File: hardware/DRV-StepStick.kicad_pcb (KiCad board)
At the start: 2 copper layers, 36.7 x 39.4 mm, 21 parts, among them J1 PCIe_Stepper, J2 Motor, J3 StepStickL, J4 StepStickR, J5 Conn_01x04, J6 SPI Mode, J7 Conn_01x02, U2 74LVC1G06

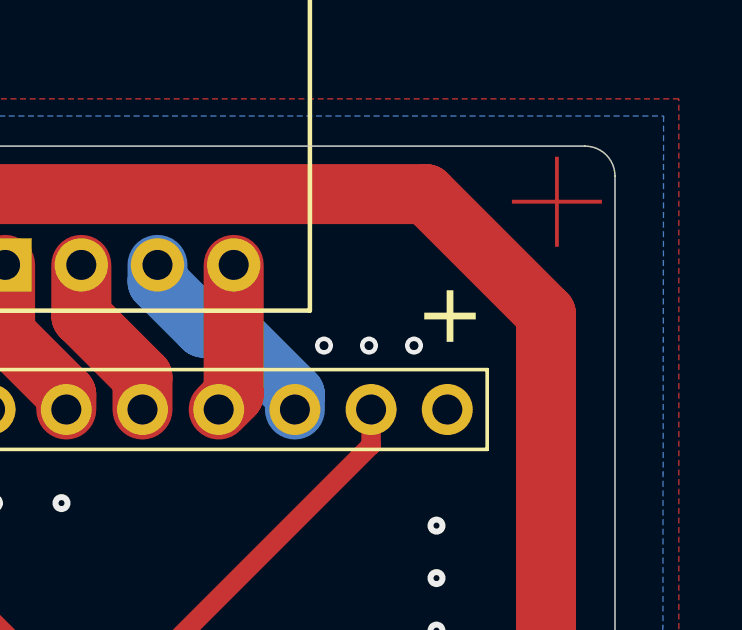
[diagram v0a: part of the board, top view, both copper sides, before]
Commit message: Removal of leftovers
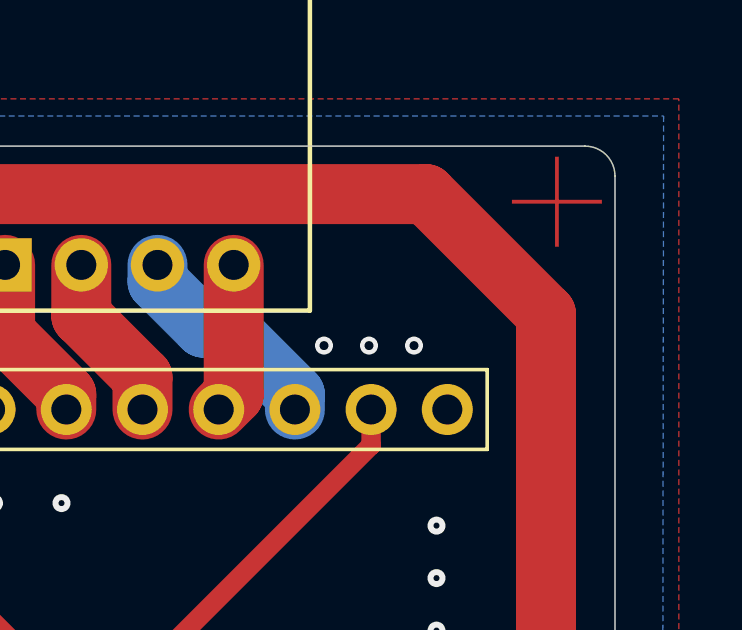
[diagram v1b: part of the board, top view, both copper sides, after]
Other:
- board text removed: "+"
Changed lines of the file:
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@@
     (effects (font (size 0.5 0.5) (thickness 0.125)))
-  )
-  (gr_text "+" (at 140.2 80.2) (layer "F.SilkS")
-    (effects (font (size 2 2) (thickness 0.5)))
   )
   (gr_text "MS1" (at 119.75 85.75 90) (layer "F.SilkS")

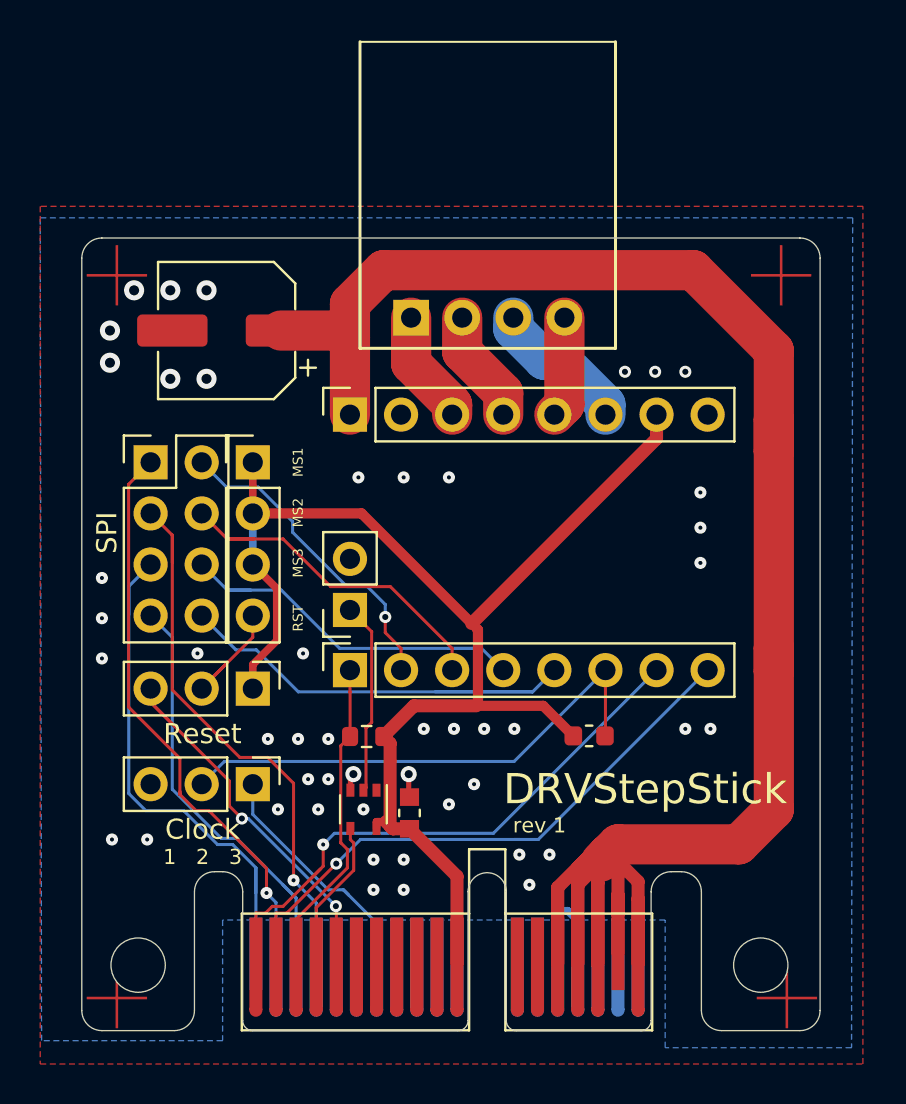
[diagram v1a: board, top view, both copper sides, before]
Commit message: Update of PCBs
- added tooling holes
- added order number location under components

Updated projects:
- DRV-Stepstick
- TMC2209
- TMC2130
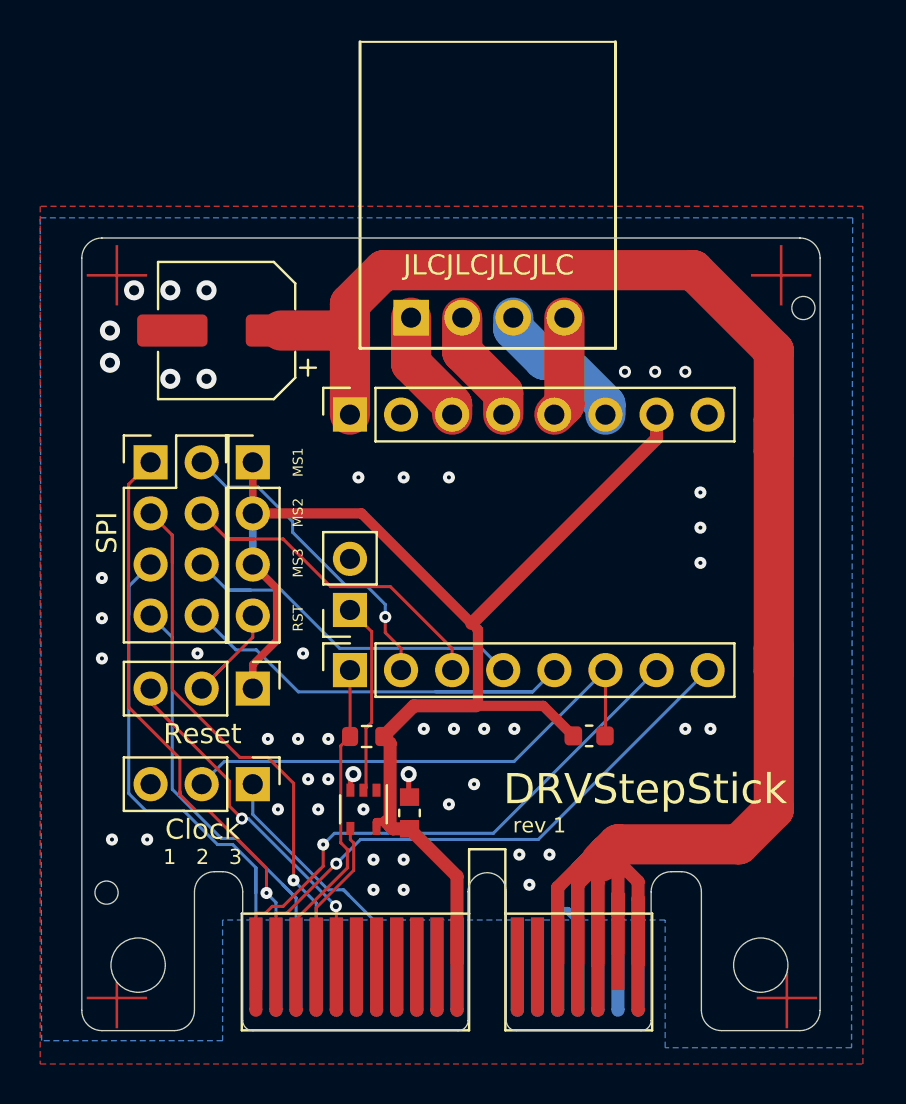
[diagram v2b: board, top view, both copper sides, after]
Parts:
- added H3: JLC Tooling Hole, PrntrBoardV2:JLC_Tool_hole, F.Cu at (100.8, 107.9)
- added H4: JLC Tooling Hole, PrntrBoardV2:JLC_Tool_hole, F.Cu at (102.9, 107.9)
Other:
- board text added: "JLCJLCJLCJLC"
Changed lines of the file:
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@@
     )
+  )
+  (footprint "PrntrBoardV2:JLC_Tool_hole" (layer "F.Cu")
+    (at 102.9 107.92)
+    (property "Sheet file" "DRV-StepStick.kicad_sch")
+    (property "Sheet name" "")
+    (property "exclude_from_bom" "")
+    (attr exclude_from_bom)
+    (fp_text reference "H4" (at 0 0.5 unlocked) (layer "F.SilkS") hide
+      (effects (font (size 1 1) (thickness 0.15)))
+    )
+    (fp_text value "JLC Tooling Hole" (at 0 -0.5 unlocked) (layer "F.Fab")
+      (effects (font (size 1 1) (thickness 0.15)))
+    )
+    (pad "" np_thru_hole circle (at 41.97 -29.84) (size 1.152 1.152) (drill 1.152) (layers *.Cu *.Mask)
+      (solder_mask_margin 0.148) (clearance 0.148))
   )
   (footprint "Connector_PinHeader_2.54mm:PinHeader_2x04_P2.54mm_Vertical" (layer "F.Cu")
@@
       (rotate (xyz 0 0 0))
     )
+  )
+  (footprint "PrntrBoardV2:JLC_Tool_hole" (layer "F.Cu")
+    (at 100.75 107.92)
+    (property "Sheet file" "DRV-StepStick.kicad_sch")
+    (property "Sheet name" "")
+    (property "exclude_from_bom" "")
+    (attr exclude_from_bom)
+    (fp_text reference "H3" (at 0 0.5 unlocked) (layer "F.SilkS") hide
+      (effects (font (size 1 1) (thickness 0.15)))
+    )
+    (fp_text value "JLC Tooling Hole" (at 0 -0.5 unlocked) (layer "F.Fab")
+      (effects (font (size 1 1) (thickness 0.15)))
+    )
+    (pad "" np_thru_hole circle (at 9.48 -0.78) (size 1.152 1.152) (drill 1.152) (layers *.Cu *.Mask)
+      (solder_mask_margin 0.148) (clearance 0.148))
   )
   (footprint "Connector_PinHeader_2.54mm:PinHeader_1x03_P2.54mm_Vertical" (layer "F.Cu")
@@
     (effects (font (size 1 1) (thickness 0.15)))
   )
+  (gr_text "JLCJLCJLCJLC" (at 129.23 75.95) (layer "F.SilkS")
+    (effects (font (size 1 1) (thickness 0.1)))
+  )
   (gr_text "1   2   3" (at 115.003756 105.368139) (layer "F.SilkS")
